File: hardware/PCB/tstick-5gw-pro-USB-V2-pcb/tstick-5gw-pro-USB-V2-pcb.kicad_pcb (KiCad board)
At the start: 4 copper layers, 53.3 x 25.4 mm, 66 parts, among them J1 USB_C_Receptacle_USB2.0, Q1 BSS138, Q2 BSS138, Q3 BSS138, SW1 B3U-1000P, SW2 B3U-1000P, U1 USBLC6-2P6, U2 MCP73871, U3 NCP167AMX330TBG, U4 NCP167AMX180TBG

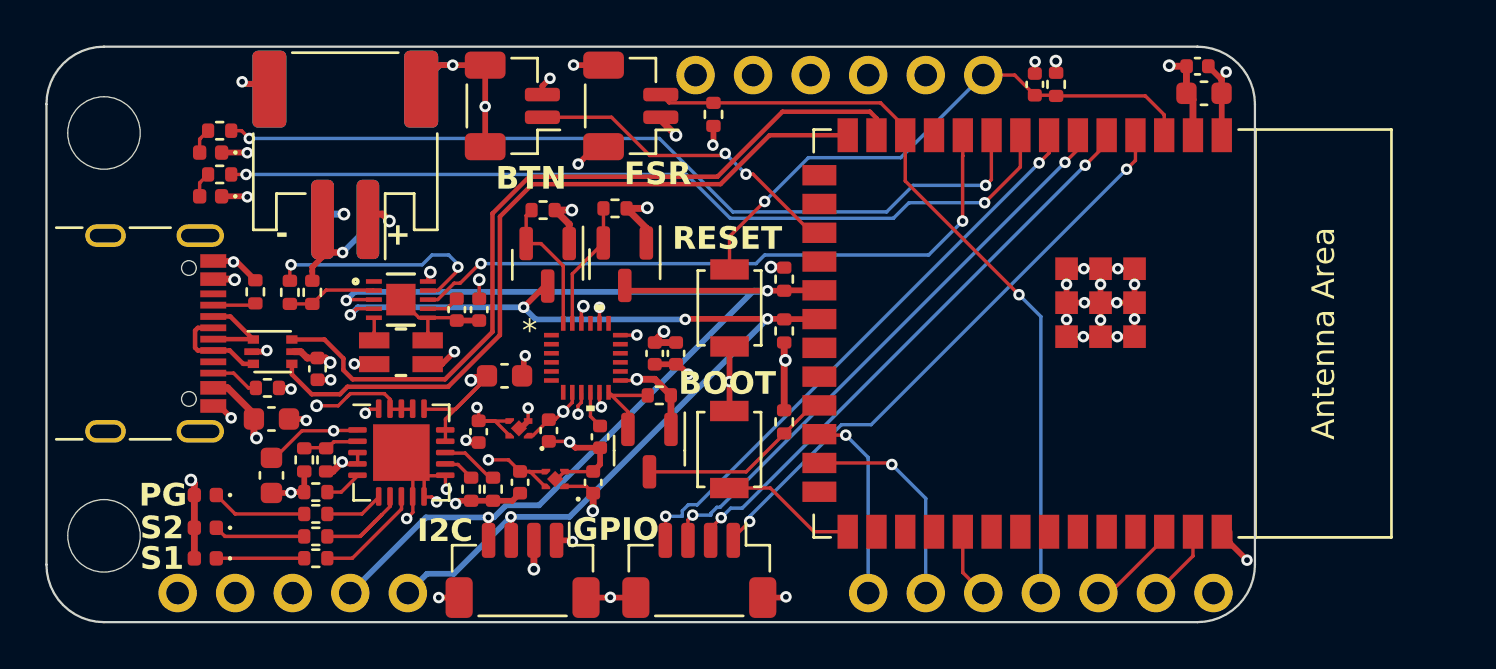
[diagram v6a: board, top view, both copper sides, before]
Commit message: increased PCB board length, updated LEDs
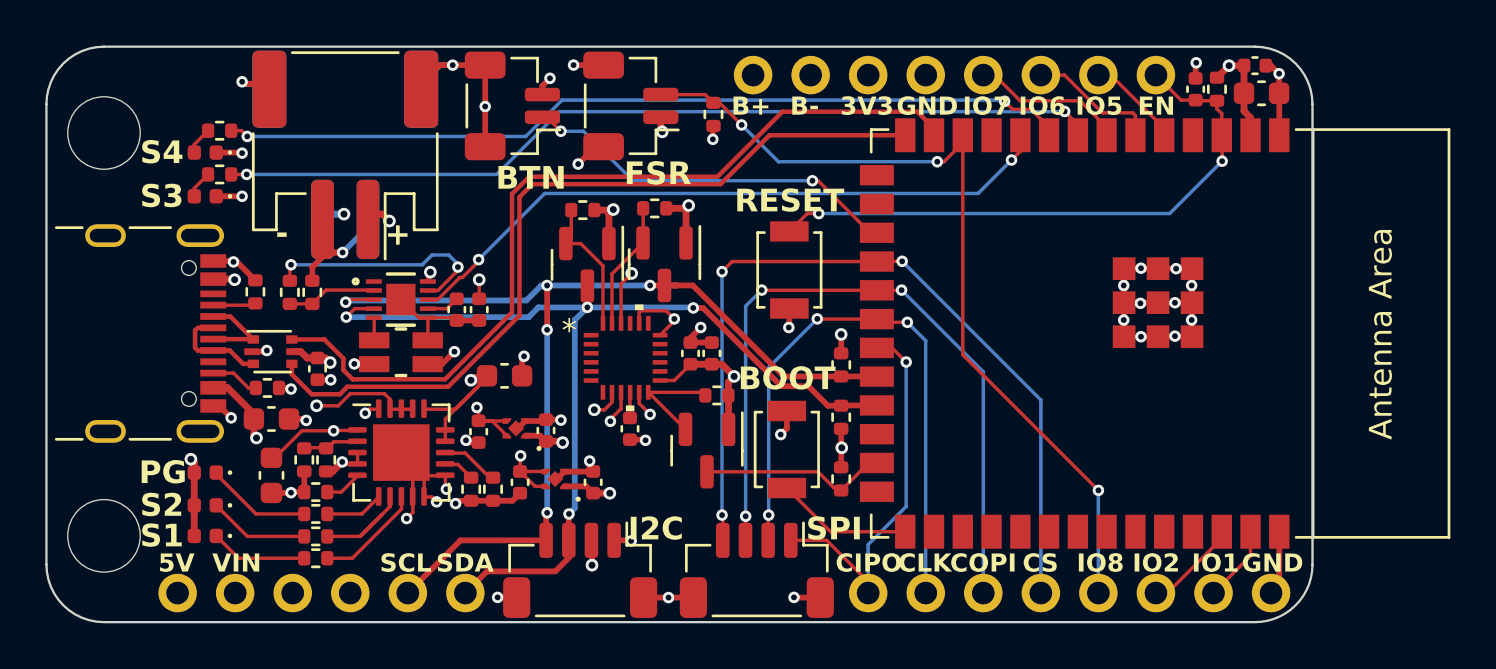
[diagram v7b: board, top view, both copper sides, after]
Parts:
- moved C9 7.10 mm to (143.4, 50.1)
- moved R5 7.10 mm to (144.4, 50.1)
- moved R16 4.57 mm to (127.8, 64.6)
- moved R19 4.54 mm to (127.8, 62.3)
- moved R23 3.56 mm to (127.8, 67.3)
- moved SW2 3.13 mm to (125.5, 58.1)
- moved C19 2.54 mm to (146.1, 49.1)
- moved C13 2.54 mm to (146.3, 50.3)
- moved MCU1 2.54 mm to (138.9, 60.9)
- moved R21 2.54 mm to (122.3, 63.7)
- moved SW1 2.54 mm to (125.4, 66.0)
- moved TOUCH1 2.54 mm to (116.3, 71.4)
- moved BOARDLAYOUT1 2.54 mm to (134.1, 49.5)
- moved Q3 2.54 mm to (121.9, 66.1)
- moved TOUCH2 2.54 mm to (124.1, 71.4)
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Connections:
- MCU1 pad 15: /IO3 -> unconnected-(MCU1-GPIO3/TOUCH3/ADC1_CH2-Pad15)
- MCU1 pad 16: /IO46 -> unconnected-(MCU1-GPIO46-Pad16)
- MCU1 pad 18: /IO10 -> /CS
- MCU1 pad 19: /SCL -> /COPI
- MCU1 pad 20: /SDA -> /SCLK
- MCU1 pad 21: /IO13 -> /CIPO
- MCU1 pad 22: /IO14 -> /SCL
- MCU1 pad 23: /IO21 -> /SDA
- MCU1 pad 24: /CIPO -> unconnected-(MCU1-GPIO47/SPICLK_P/SUBSPICLK_P_DIFF-Pad24)
- MCU1 pad 25: /SCK -> /IO48
- MCU1 pad 26: /IO45 -> unconnected-(MCU1-GPIO45-Pad26)
- MCU1 pad 31: /COPI -> unconnected-(MCU1-GPIO38/FSPIWP/SUBSPIWP-Pad31)
- Q3 pad 3: /IO21 -> /IO48
- R23 pad 1: /IO21 -> /IO48
- TOUCH2 pad 1: /IO4 -> /CIPO
- TOUCH2 pad 2: /IO5 -> /SCLK
- TOUCH2 pad 3: /IO6 -> /COPI
- TOUCH2 pad 4: /IO7 -> /CS
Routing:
- net /CS: track 0.00 -> 37.2 mm, vias 0 -> 3
- net SYS: track 41.0 -> 11.3 mm
- net /COPI: track 3.08 -> 32.4 mm, vias 0 -> 3
- net /SCLK: track 0.00 -> 27.0 mm, vias 0 -> 3
- net /IO4: track 26.0 -> 0.00 mm, vias 2 -> 0
- net /IO5: track 25.4 -> 4.18 mm, vias 2 -> 0
- net /IO6: track 25.6 -> 5.78 mm, vias 2 -> 0
- net /IO7: track 25.6 -> 6.75 mm, vias 2 -> 0
- net /SCK: track 9.52 -> 0.00 mm, vias 1 -> 0
- net /IO21: track 8.71 -> 0.00 mm
- net /CIPO: track 8.56 -> 17.1 mm
- net /IO48: track 0.00 -> 8.34 mm
- net /SCL: track 53.7 -> 45.6 mm, vias 3 -> 5
- net /IO8: track 34.4 -> 37.9 mm, vias 1 -> 3
- net /USBD+: track 33.2 -> 35.7 mm
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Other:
- board size 53.3 x 25.4 mm -> 55.9 x 25.4 mm
- board text added: "3V3"
- board text added: "B+"
- board text added: "B-"
- board text added: "CIPO"
- board text added: "CLK"
- board text added: "COPI"
- board text added: "CS"
- board text added: "EN"
- board text added: "EVT1 = IO10 EVT2 = IO11 EVT3 = IO12 EVT4 = IO13"
- board text added: "GND"
- board text added: "IO1"
- board text added: "IO2"
- board text added: "IO5"
- board text added: "IO6"
- board text added: "IO7"
- board text added: "IO8"
- board text added: "S3"
- board text added: "S4"
- board text added: "SCL"
- board text added: "SDA"
- board text added: "SPI"
- board text added: "VIN"
- board text removed: "EVT1 = IO7 EVT2 = IO6 EVT3 = IO5 EVT4 = IO4"
- board text removed: "GPIO"
